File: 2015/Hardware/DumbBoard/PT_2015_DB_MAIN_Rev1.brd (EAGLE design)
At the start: 137.2 x 166.4 mm, 69 parts, among them Q12 2N7002

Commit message: Fixed some issues
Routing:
- net 12V-SIG: track 65.7 -> 0.00 mm, vias 1 -> 0
- net +5V: track 515.7 -> 489.9 mm, vias 7 -> 6
- net V_BATT: track 312.1 -> 291.0 mm
- removed copper zone on layer 1, net N$40
- removed copper zone on layer 1, net N$41
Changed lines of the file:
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@@
 <?xml version="1.0" encoding="utf-8"?>
 <!DOCTYPE eagle SYSTEM "eagle.dtd">
-<eagle version="7.1.0">
+<eagle version="7.0.0">
 <drawing>
 <settings>
@@
 <vertex x="40.64" y="21.59"/>
 <vertex x="45.72" y="21.59"/>
-<vertex x="45.72" y="11.43"/>
-<vertex x="40.64" y="11.43"/>
-<vertex x="40.64" y="5.08"/>
-<vertex x="45.72" y="5.08"/>
-<vertex x="51.054" y="-2.667"/>
+<vertex x="45.72" y="8.89"/>
+<vertex x="3.81" y="8.89"/>
+<vertex x="2.54" y="7.62"/>
+<vertex x="2.54" y="2.54"/>
+<vertex x="3.81" y="1.27"/>
+<vertex x="45.72" y="1.27"/>
+<vertex x="49.784" y="-2.667"/>
 <vertex x="81.28" y="-2.54"/>
 <vertex x="81.28" y="101.6"/>
@@
 <contactref element="MOTOR_6" pad="R2"/>
 <contactref element="R24" pad="1"/>
-<wire x1="5.08" y1="5.08" x2="12.7" y2="5.08" width="0.4064" layer="16"/>
-<wire x1="12.7" y1="5.08" x2="14.1" y2="5.08" width="0.4064" layer="16"/>
-<wire x1="14.1" y1="5.08" x2="16.51" y2="7.49" width="0.4064" layer="16"/>
-<wire x1="16.51" y1="7.49" x2="21.46" y2="7.49" width="0.4064" layer="16"/>
-<wire x1="21.46" y1="7.49" x2="24.13" y2="10.16" width="0.4064" layer="16"/>
 <wire x1="24.13" y1="10.16" x2="24.13" y2="16.38" width="0.4064" layer="16"/>
 <wire x1="24.13" y1="16.38" x2="16.51" y2="24" width="0.4064" layer="16"/>
@@
 <wire x1="16.51" y1="40.51" x2="16.51" y2="40.51" width="0" layer="19" extent="1-16"/>
 <wire x1="16.51" y1="24" x2="16.51" y2="24" width="0" layer="19" extent="1-16"/>
-<wire x1="16.51" y1="7.49" x2="16.51" y2="7.49" width="0" layer="19" extent="1-16"/>
 </signal>
 <signal name="+5V">
@@
 <wire x1="121.793" y1="31.623" x2="105.41" y2="31.496" width="0.8128" layer="1"/>
 <wire x1="105.41" y1="31.496" x2="103.759" y2="33.147" width="0.8128" layer="1"/>
-<wire x1="103.759" y1="33.147" x2="103.759" y2="37.846" width="0.8128" layer="1"/>
-<wire x1="103.759" y1="37.846" x2="102.362" y2="39.243" width="0.8128" layer="16"/>
-<wire x1="102.362" y1="39.243" x2="88.265" y2="39.243" width="0.8128" layer="16"/>
-<wire x1="106.683" y1="40.77" x2="103.759" y2="37.846" width="0.4064" layer="1"/>
 <wire x1="128.905" y1="11.43" x2="128.905" y2="11.315" width="0.4064" layer="16"/>
 <wire x1="121.793" y1="31.623" x2="125.476" y2="27.94" width="0.8128" layer="16"/>
@@
 <wire x1="33.02" y1="119.38" x2="31.75" y2="119.38" width="0.4064" layer="1"/>
 <wire x1="31.75" y1="119.38" x2="31.75" y2="120.396" width="0.4064" layer="1"/>
-<via x="103.759" y="37.846" extent="1-16" drill="0.5"/>
-<wire x1="88.265" y1="39.243" x2="87.63" y2="39.878" width="0.8128" layer="16"/>
 <wire x1="130.81" y1="113.03" x2="135.89" y2="113.03" width="0.4064" layer="16"/>
 <contactref element="L1" pad="8"/>
@@
 <wire x1="10.668" y1="138.43" x2="10.668" y2="140.97" width="0.4064" layer="1"/>
 </signal>
-<signal name="N$40">
-<polygon width="0.4064" layer="1" thermals="no" rank="3">
-<vertex x="25.4" y="13.97"/>
-<vertex x="36.576" y="13.97"/>
-<vertex x="40.386" y="10.16"/>
-<vertex x="40.386" y="5.588"/>
-<vertex x="36.322" y="1.524"/>
-<vertex x="25.4" y="1.524"/>
-</polygon>
-</signal>
-<signal name="N$41">
-<polygon width="0.4064" layer="1" thermals="no">
-<vertex x="3.81" y="4.064"/>
-<vertex x="3.81" y="6.096"/>
-<vertex x="5.334" y="7.62"/>
-<vertex x="22.098" y="7.62"/>
-<vertex x="23.622" y="6.096"/>
-<vertex x="23.622" y="4.064"/>
-<vertex x="22.098" y="2.54"/>
-<vertex x="5.334" y="2.54"/>
-</polygon>
-</signal>
 <signal name="N$39">
 <contactref element="R9" pad="2"/>
@@
 <signal name="12V-SIG">
 <contactref element="R15" pad="2"/>
-<wire x1="91.821" y1="50.927" x2="91.821" y2="94.742" width="0.4064" layer="1"/>
-<wire x1="94.107" y1="97.028" x2="107.29" y2="97.028" width="0.4064" layer="1"/>
-<wire x1="91.821" y1="50.927" x2="92.202" y2="50.546" width="0.4064" layer="1"/>
-<via x="92.202" y="50.546" extent="1-16" drill="0.3302"/>
-<wire x1="92.202" y1="50.546" x2="92.202" y2="47.371" width="0.4064" layer="16"/>
-<wire x1="94.107" y1="97.028" x2="91.821" y2="94.742" width="0.4064" layer="1"/>
-<wire x1="107.29" y1="97.028" x2="107.29" y2="98.756" width="0.4064" layer="1"/>
-<wire x1="107.29" y1="98.756" x2="107.315" y2="98.781" width="0.4064" layer="1"/>
 </signal>
 <signal name="N$28">

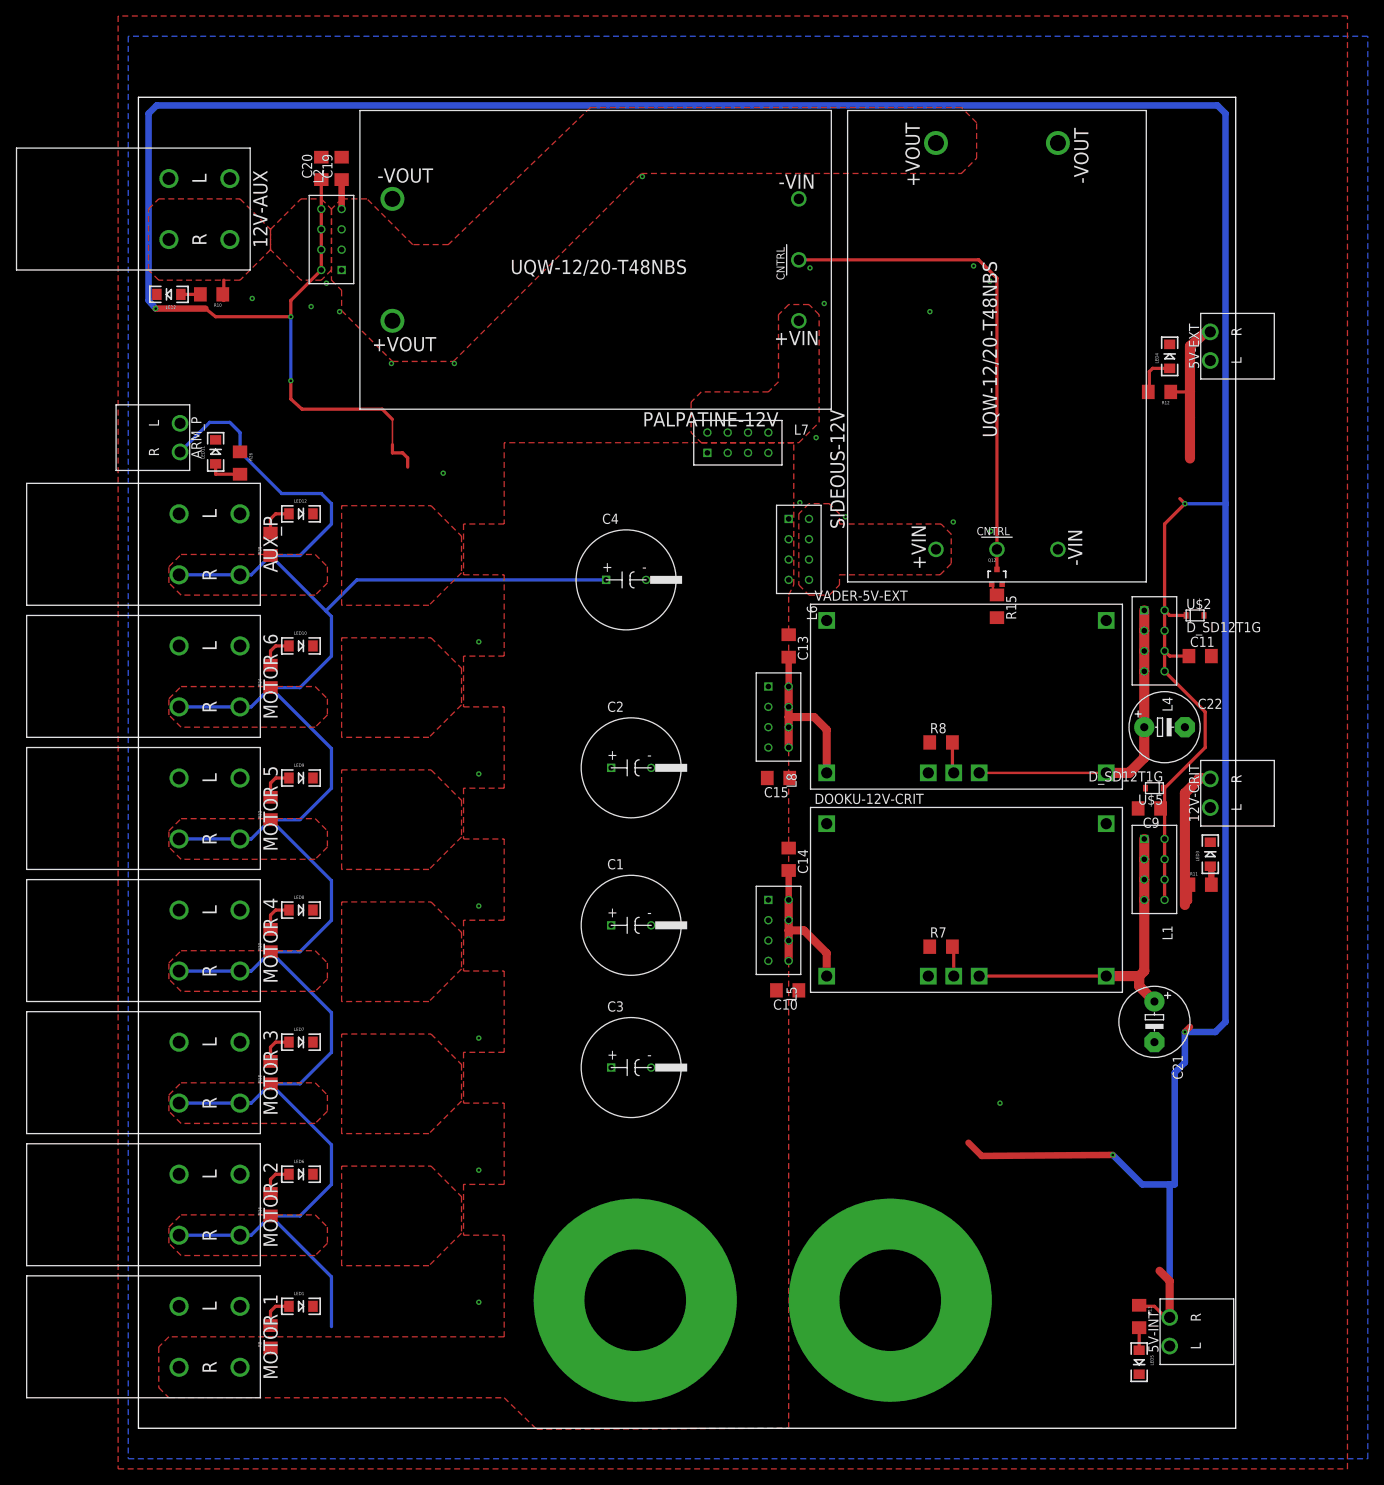
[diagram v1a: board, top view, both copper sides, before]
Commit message: Dumb Board - Attempt 2
Fixed schematic and rerouted
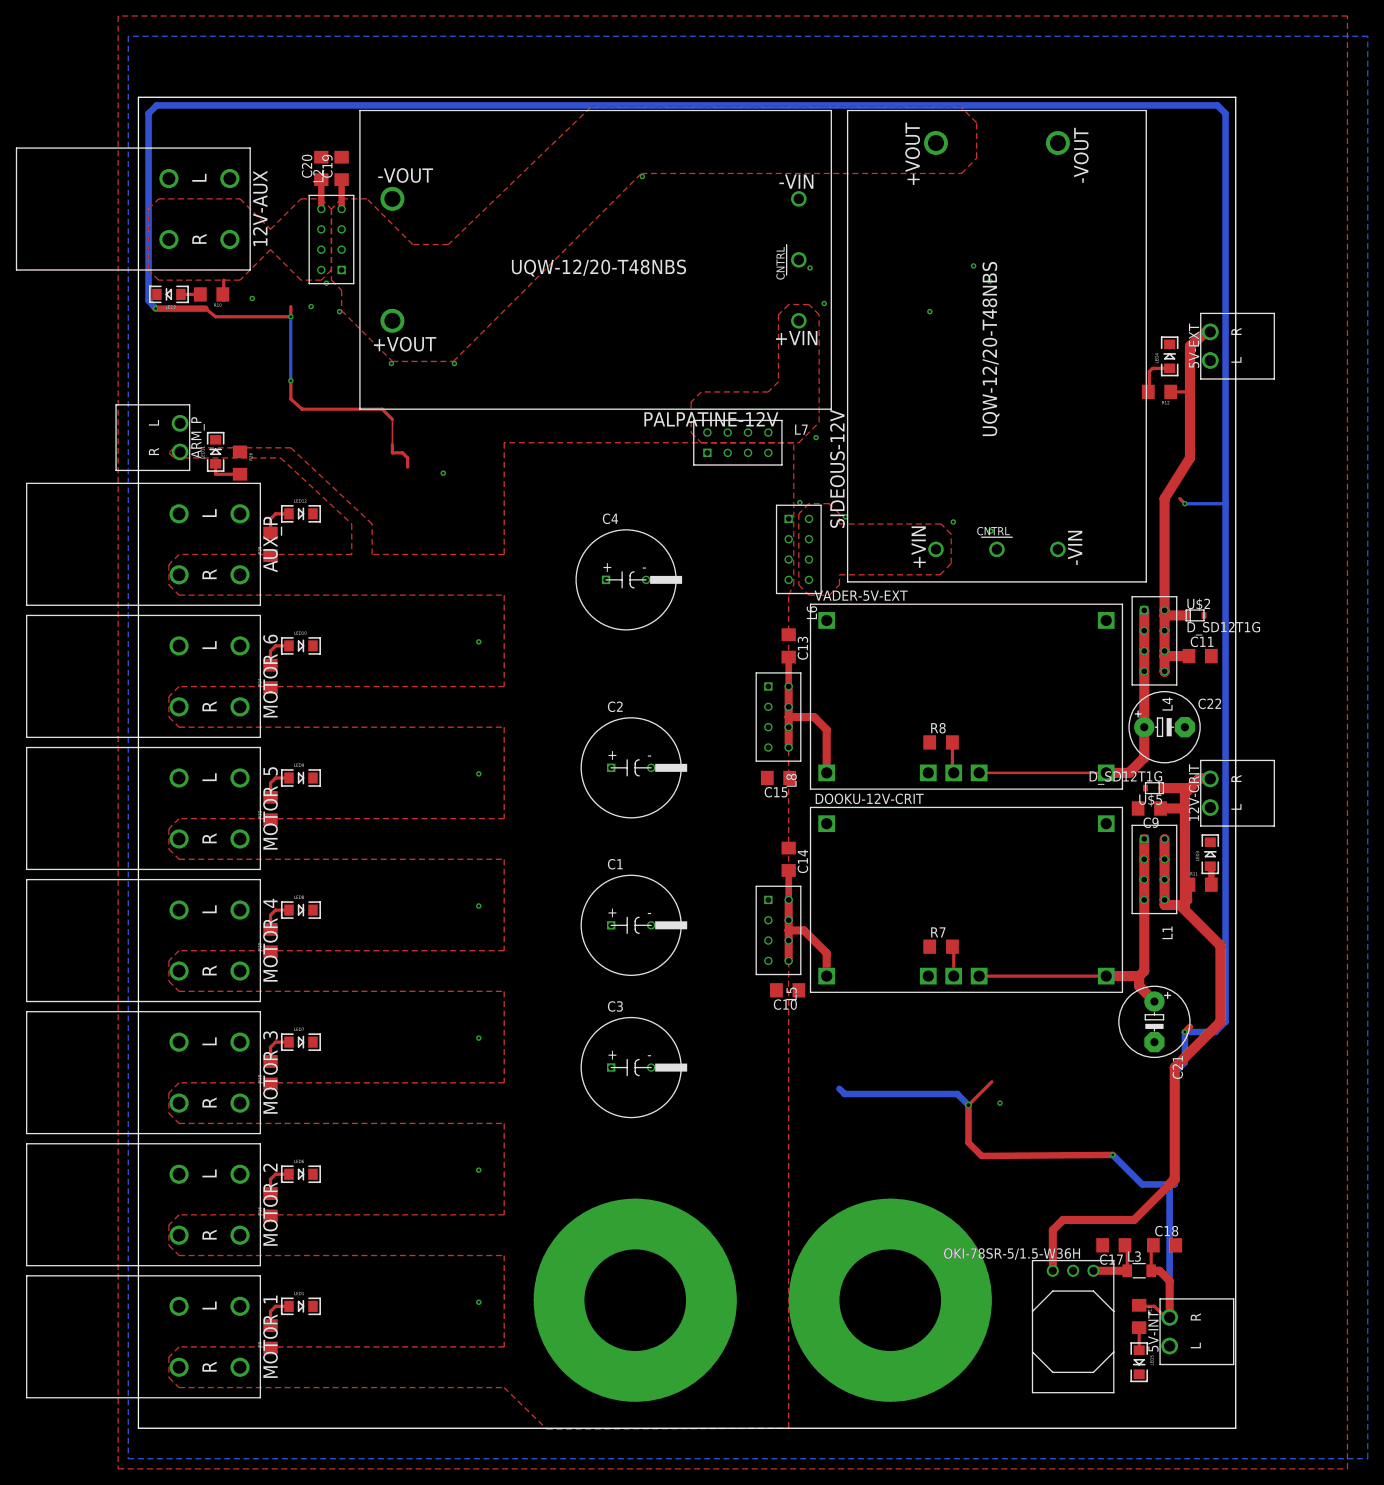
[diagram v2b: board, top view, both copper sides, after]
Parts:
- removed Q12: 2N7002, SparkFun-DiscreteSemi:SOT323
- removed R15: (no value), resistor:R1206
- added C17, C18: 47µF, resistor:C1206
- added L3: (no value), resistor:L3216C
- added OKI-78SR-5/1.5-W36H: Q_OKI-78SR, MRDT-2015-PowerBoard:OKI-78SRH
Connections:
- removed net 12V-SIG: R15.2
- removed net N$114: Q12.1, R15.1
- removed net N$4: PALPATINE-12V.2, Q12.3, SIDEOUS-12V.2
- new net N$100: C17.1, L3.1, OKI-78SR-5/1.5-W36H.3
- net +5V: now also C18.1, L3.2; no longer C11.1, C20.1, C9.1, L1.5, L1.6, L1.7, L1.8, L2.5, L2.6, L2.7, L2.8, L4.5, L4.6, L4.7, L4.8, U$2.1, U$5.1
- net 12V-AUX: now also C20.1, L2.5, L2.6, L2.7, L2.8
- net 12V-CRIT: now also C9.1, L1.5, L1.6, L1.7, L1.8, OKI-78SR-5/1.5-W36H.1, U$5.1
- net 5V-EXT: now also C11.1, L4.5, L4.6, L4.7, L4.8, U$2.1
- net GND: now also C17.2, C18.2, OKI-78SR-5/1.5-W36H.2; no longer Q12.2
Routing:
- net V_BATT: track 291.0 -> 0.00 mm
- net 12V-CRIT: track 20.9 -> 99.8 mm
- net N$4: track 62.1 -> 0.00 mm
- net +5V: track 489.9 -> 441.3 mm, vias 6 -> 7
- net 5V-EXT: track 19.7 -> 53.0 mm
- net N$100: track 0.00 -> 7.50 mm
- net 12V-AUX: track 3.31 -> 6.99 mm
- net N$114: track 1.96 -> 0.00 mm
- removed copper zone on layer 1, net N$11
- removed copper zone on layer 1, net N$28
- removed copper zone on layer 1, net N$29
- removed copper zone on layer 1, net N$44
- removed copper zone on layer 1, net N$45
- removed copper zone on layer 1, net N$54
- removed copper zone on layer 1, net N$55
- removed copper zone on layer 1, net N$60
- removed copper zone on layer 1, net N$61
- removed copper zone on layer 1, net N$66
- removed copper zone on layer 1, net N$67
- removed copper zone on layer 1, net N$78
- removed copper zone on layer 1, net N$79
